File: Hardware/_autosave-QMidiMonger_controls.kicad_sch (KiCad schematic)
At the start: 26 parts, among them J1 CV_Out, J10 Conn_01x04, J2 CV_Out, J20 Conn_01x09_Female, J21 Conn_01x08_Female, J22 Conn_01x08_Female, J23 Conn_01x03_Female, J3 CV_Out, J4 Gate_Out, J5 Gate_Out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

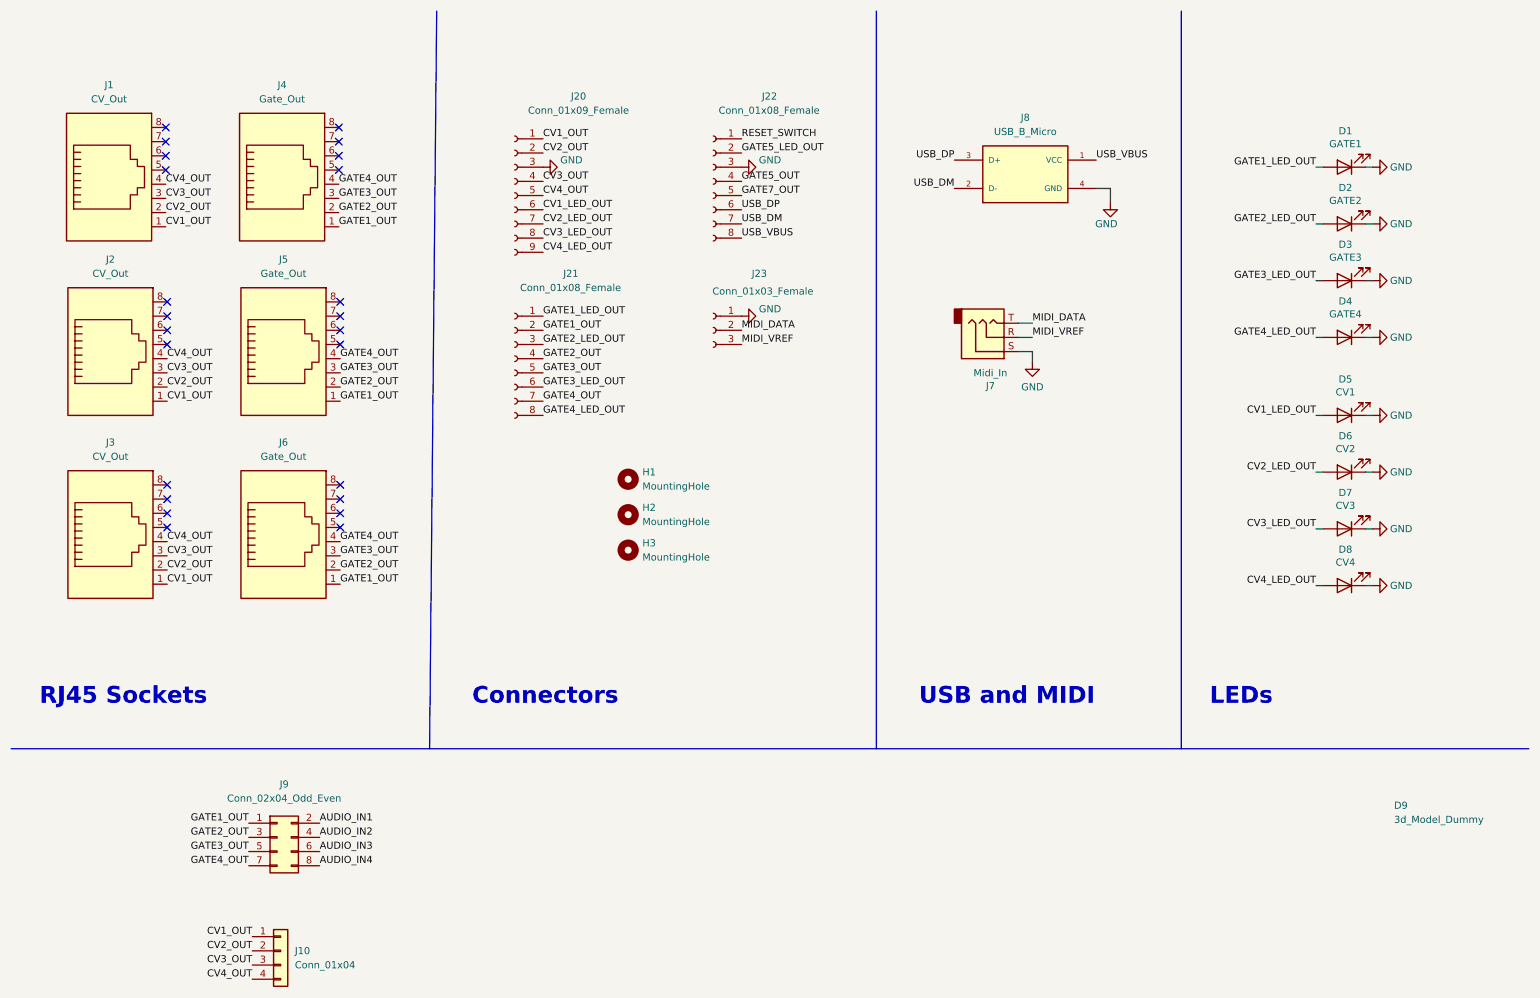
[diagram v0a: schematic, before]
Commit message: Added panel PCB; added board interconnects
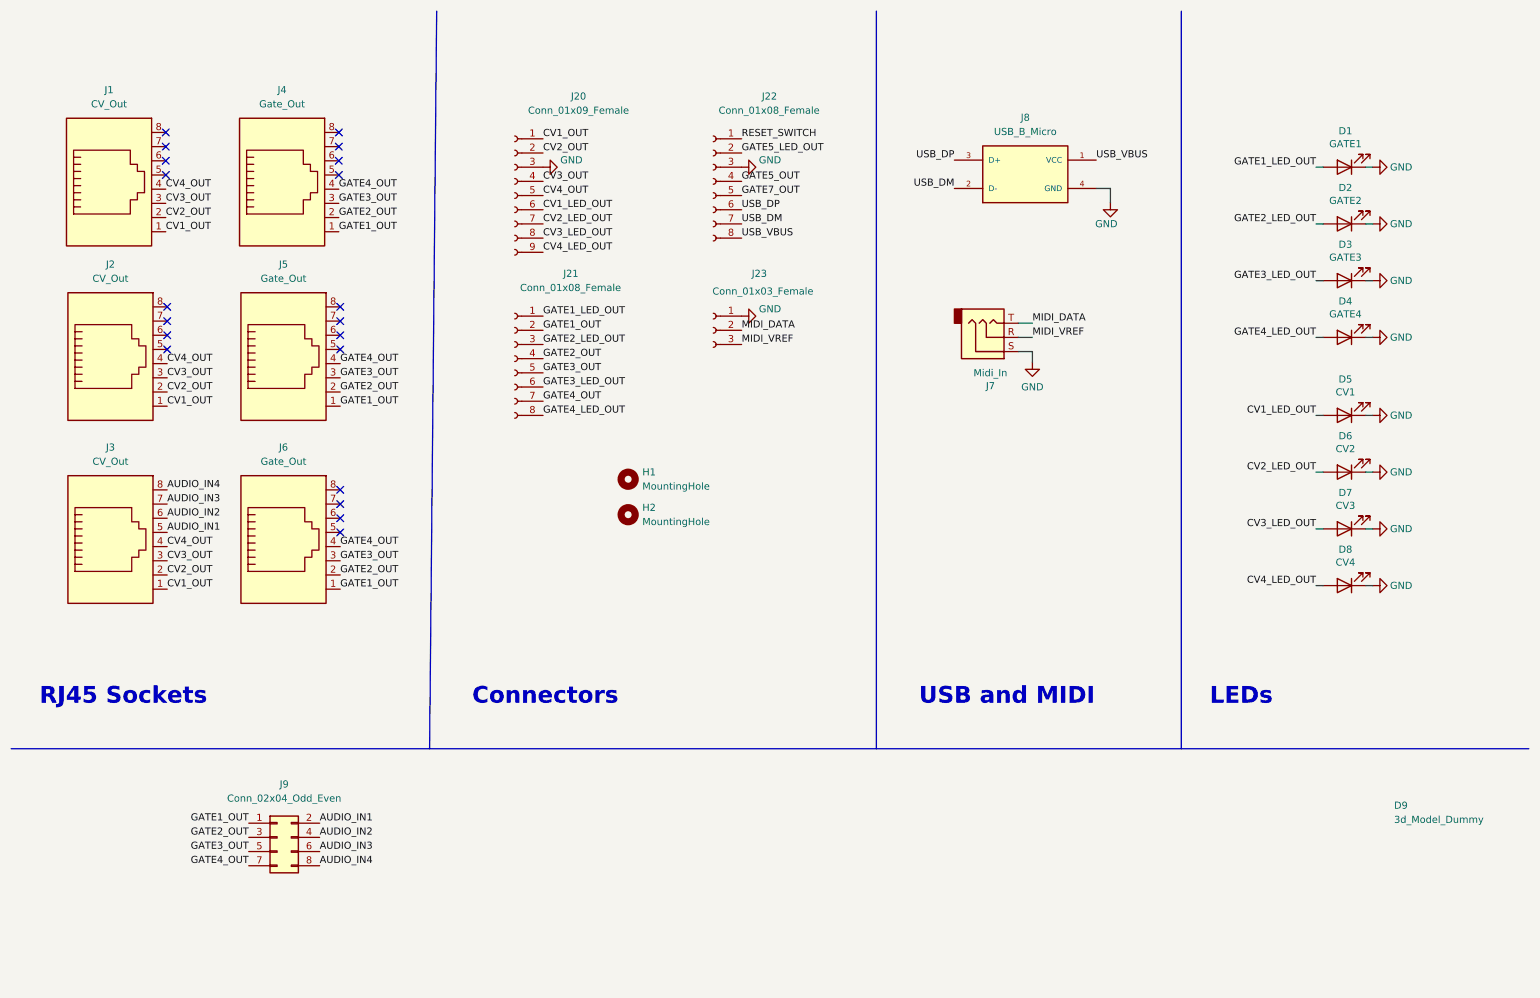
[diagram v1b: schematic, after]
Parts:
- removed H3: MountingHole, MountingHole:MountingHole_3.2mm_M3_ISO14580, symbol Mechanical:MountingHole
- removed J10: Conn_01x04, Connector_PinHeader_2.54mm:PinHeader_1x04_P2.54mm_Vertical, symbol Connector_Generic:Conn_01x04
- J23: footprint (none) -> Connector_PinHeader_2.54mm:PinHeader_1x03_P2.54mm_Vertical
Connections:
- net AUDIO_IN1: now also J3.5
- net AUDIO_IN2: now also J3.6
- net AUDIO_IN3: now also J3.7
- net AUDIO_IN4: now also J3.8
- no-connect marks 24 -> 20
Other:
- moved on the sheet: J1, J2, J3, J4, J5, J6
